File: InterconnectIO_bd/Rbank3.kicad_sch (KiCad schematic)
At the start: 48 parts, among them K33 TQ2-5, K34 TQ2-5, K35 TQ2-5, K36 TQ2-5, K37 TQ2-5, K38 TQ2-5, K39 TQ2-5, K40 TQ2-5, K41 TQ2-5

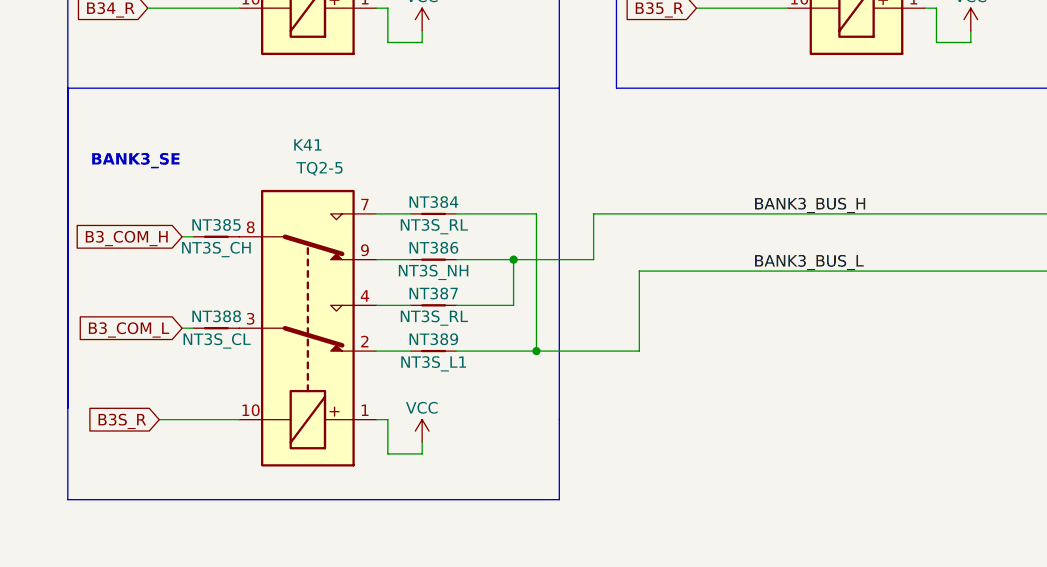
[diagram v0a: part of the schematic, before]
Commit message: Reverse COM_H and COM_L on relay Bank
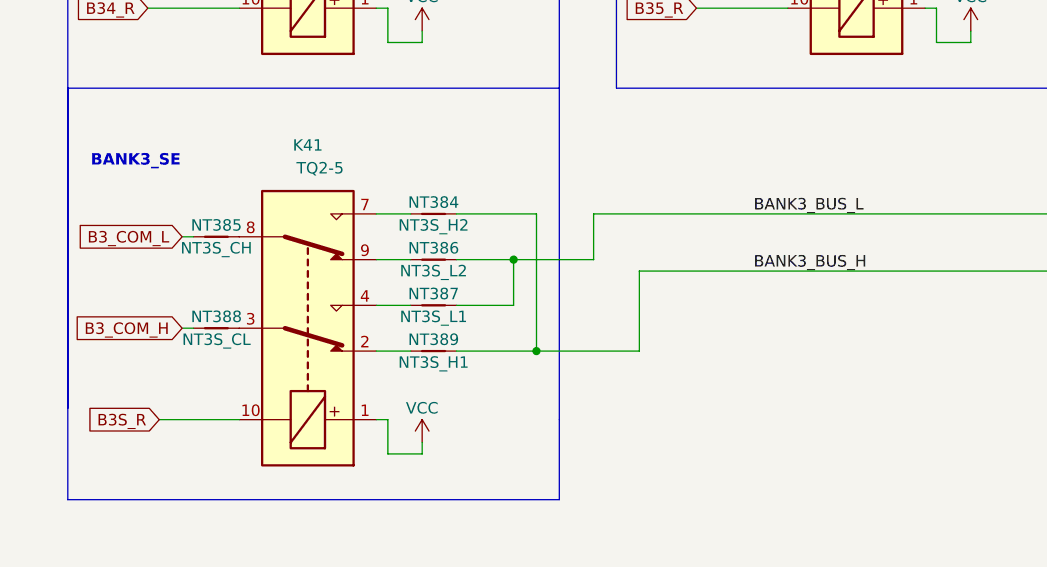
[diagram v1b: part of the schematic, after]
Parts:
- NT384: value NT3S_RL -> NT3S_H2
- NT386: value NT3S_NH -> NT3S_L2
- NT387: value NT3S_RL -> NT3S_L1
- NT389: value NT3S_L1 -> NT3S_H1
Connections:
- net B3_COM_H: now also NT388.1; no longer NT385.1
- net B3_COM_L: now also NT385.1; no longer NT388.1
- net BANK3_BUS_H: now also NT368.1, NT369.1, NT370.1, NT371.1, NT376.1, NT377.1, NT378.1, NT379.1, NT384.2, NT389.2; no longer NT372.1, NT373.1, NT374.1, NT375.1, NT380.1, NT381.1, NT382.1, NT383.1, NT386.2, NT387.2
- net BANK3_BUS_L: now also NT372.1, NT373.1, NT374.1, NT375.1, NT380.1, NT381.1, NT382.1, NT383.1, NT386.2, NT387.2; no longer NT368.1, NT369.1, NT370.1, NT371.1, NT376.1, NT377.1, NT378.1, NT379.1, NT384.2, NT389.2
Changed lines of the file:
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@@
     (effects (font (size 1.27 1.27) (thickness 0.254) bold) (justify left bottom))
   )
-  (label "BANK3_BUS_L" (at 96.52 128.27 0) (fields_autoplaced)
+  (label "BANK3_BUS_H" (at 96.52 128.27 0) (fields_autoplaced)
     (effects (font (size 1.27 1.27)) (justify left bottom))
   )
@@
     (effects (font (size 1.27 1.27)) (justify left bottom))
   )
-  (label "BANK3_BUS_H" (at 96.52 121.92 0) (fields_autoplaced)
+  (label "BANK3_BUS_L" (at 96.52 121.92 0) (fields_autoplaced)
     (effects (font (size 1.27 1.27)) (justify left bottom))
   )
@@
     (effects (font (size 1.27 1.27)) (justify left bottom))
   )
-  (global_label "B3_COM_H" (shape input) (at 33.02 124.46 180) (fields_autoplaced)
+  (global_label "B3_COM_L" (shape input) (at 33.02 124.46 180) (fields_autoplaced)
     (effects (font (size 1.27 1.27)) (justify right))
-    (property "Intersheetrefs" "${INTERSHEET_REFS}" (at 20.8098 124.3806 0)
+    (property "Intersheetrefs" "${INTERSHEET_REFS}" (at 20.6195 124.46 0)
       (effects (font (size 1.27 1.27)) (justify right) hide)
     )
@@
     )
   )
-  (global_label "B3_COM_L" (shape input) (at 33.02 134.62 180) (fields_autoplaced)
+  (global_label "B3_COM_H" (shape input) (at 33.02 134.62 180) (fields_autoplaced)
     (effects (font (size 1.27 1.27)) (justify right))
-    (property "Intersheetrefs" "${INTERSHEET_REFS}" (at 21.1121 134.5406 0)
+    (property "Intersheetrefs" "${INTERSHEET_REFS}" (at 20.3171 134.62 0)
       (effects (font (size 1.27 1.27)) (justify right) hide)
     )
@@
       (effects (font (size 1.27 1.27)))
     )
-    (property "Value" "NT3S_RL" (at 60.96 133.35 0)
+    (property "Value" "NT3S_L1" (at 60.96 133.35 0)
       (effects (font (size 1.27 1.27)))
     )
@@
       (effects (font (size 1.27 1.27)))
     )
-    (property "Value" "NT3S_RL" (at 60.96 123.19 0)
+    (property "Value" "NT3S_H2" (at 60.96 123.19 0)
       (effects (font (size 1.27 1.27)))
     )
@@
       (effects (font (size 1.27 1.27)))
     )
-    (property "Value" "NT3S_L1" (at 60.96 138.43 0)
+    (property "Value" "NT3S_H1" (at 60.96 138.43 0)
       (effects (font (size 1.27 1.27)))
     )
@@
       (effects (font (size 1.27 1.27)))
     )
-    (property "Value" "NT3S_NH" (at 60.96 128.27 0)
-      (effects (font (size 1.27 1.27)))
-    )
+    (property "Value" "NT3S_L2" (at 60.96 128.27 0)
+      (effects (font (size 1.27 1.27)))
+    )
